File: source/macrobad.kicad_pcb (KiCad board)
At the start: 2 copper layers, 105 x 60 mm, 11 parts, among them J1 Conn_01x04_Pin, SW1 SW_Push, SW2 SW_Push, SW3 SW_Push, SW4 SW_Push, SW5 SW_Push, SW6 RotaryEncoder_Switch, U2 MOUDLE-SEEEDUINO-XIAO

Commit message: wired neopixel, added some little things
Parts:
- added G***: LOGO, LOGO, B.Cu at (188.0, 128.5)
- moved 3.2mm 3.83 mm to (206.5, 142.0)
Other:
- board text added: "https://github.com/jeskodevv/macrobad"

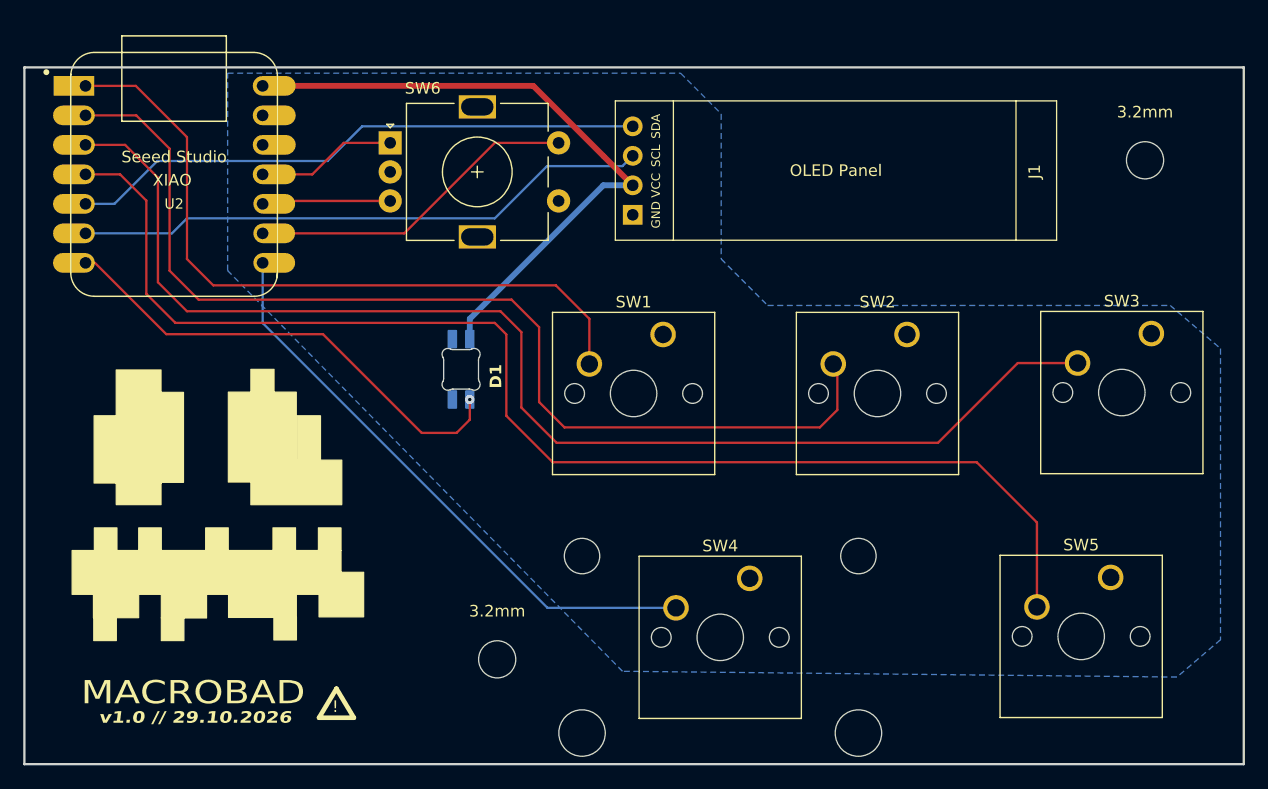
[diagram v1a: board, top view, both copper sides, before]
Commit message: PCB shrinked to 100mm
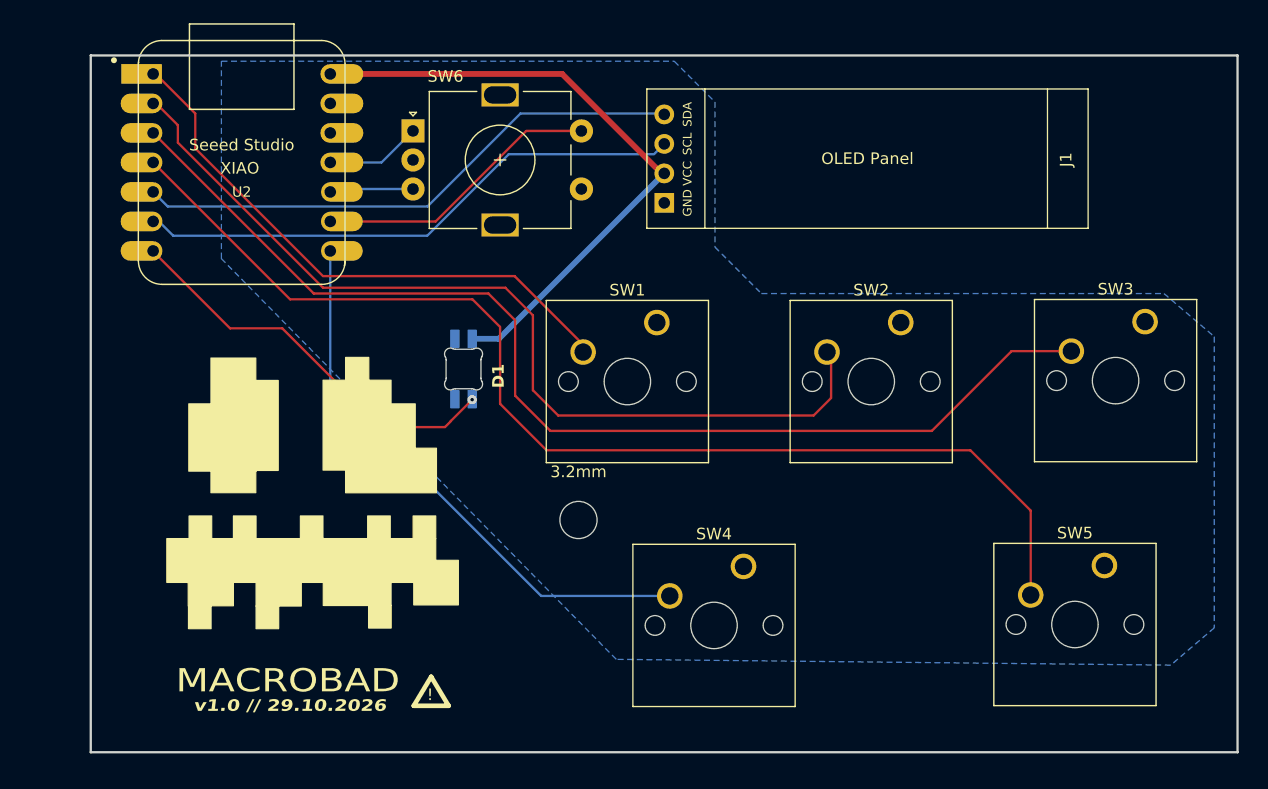
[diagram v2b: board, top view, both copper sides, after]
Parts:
- removed the 3.2mm at (262.3, 99.0)
- SW4: footprint Button_Switch_Keyboard:SW_Cherry_MX_2.00u_PCB -> Button_Switch_Keyboard:SW_Cherry_MX_1.00u_PCB
- moved 3.2mm 13.9 mm to (213.5, 130.0)
- moved G*** 8.22 mm to (196.2, 127.5)
- moved U2 5.91 mm to (184.5, 99.2)
- moved J1 2.90 mm to (257.4, 104.9)
- moved SW6 2.22 mm to (199.2, 96.5)
- moved SW5 1.16 mm to (258.8, 133.9)
- moved SW1 1.16 mm to (220.3, 113.0)
- moved SW2 1.16 mm to (241.3, 113.0)
- moved SW3 1.16 mm to (262.3, 112.9)
- moved SW4 1.16 mm to (227.7, 134.0)
- moved D1 0.22 mm to (203.5, 117.0)
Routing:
- net SW1: track 61.7 -> 49.1 mm
- net SW2: track 90.5 -> 78.9 mm
- net SW3: track 108.0 -> 96.3 mm
- net SW5: track 110.4 -> 99.1 mm
- net LED: track 41.4 -> 35.3 mm
- net RE1: track 12.1 -> 8.25 mm
- net RE2: track 11.1 -> 7.23 mm
- net RESW: track 28.7 -> 24.9 mm
- net SW4: track 50.9 -> 48.3 mm
- net SCL: track 49.9 -> 47.8 mm
- net SDA: track 49.9 -> 47.9 mm
- net VCC: track 56.0 -> 54.7 mm
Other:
- board size 105 x 60 mm -> 98.8 x 60 mm
